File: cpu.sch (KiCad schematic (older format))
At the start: 30 parts, among them P27 BDM, U1 MC9S12XDP512, X1 16MHz

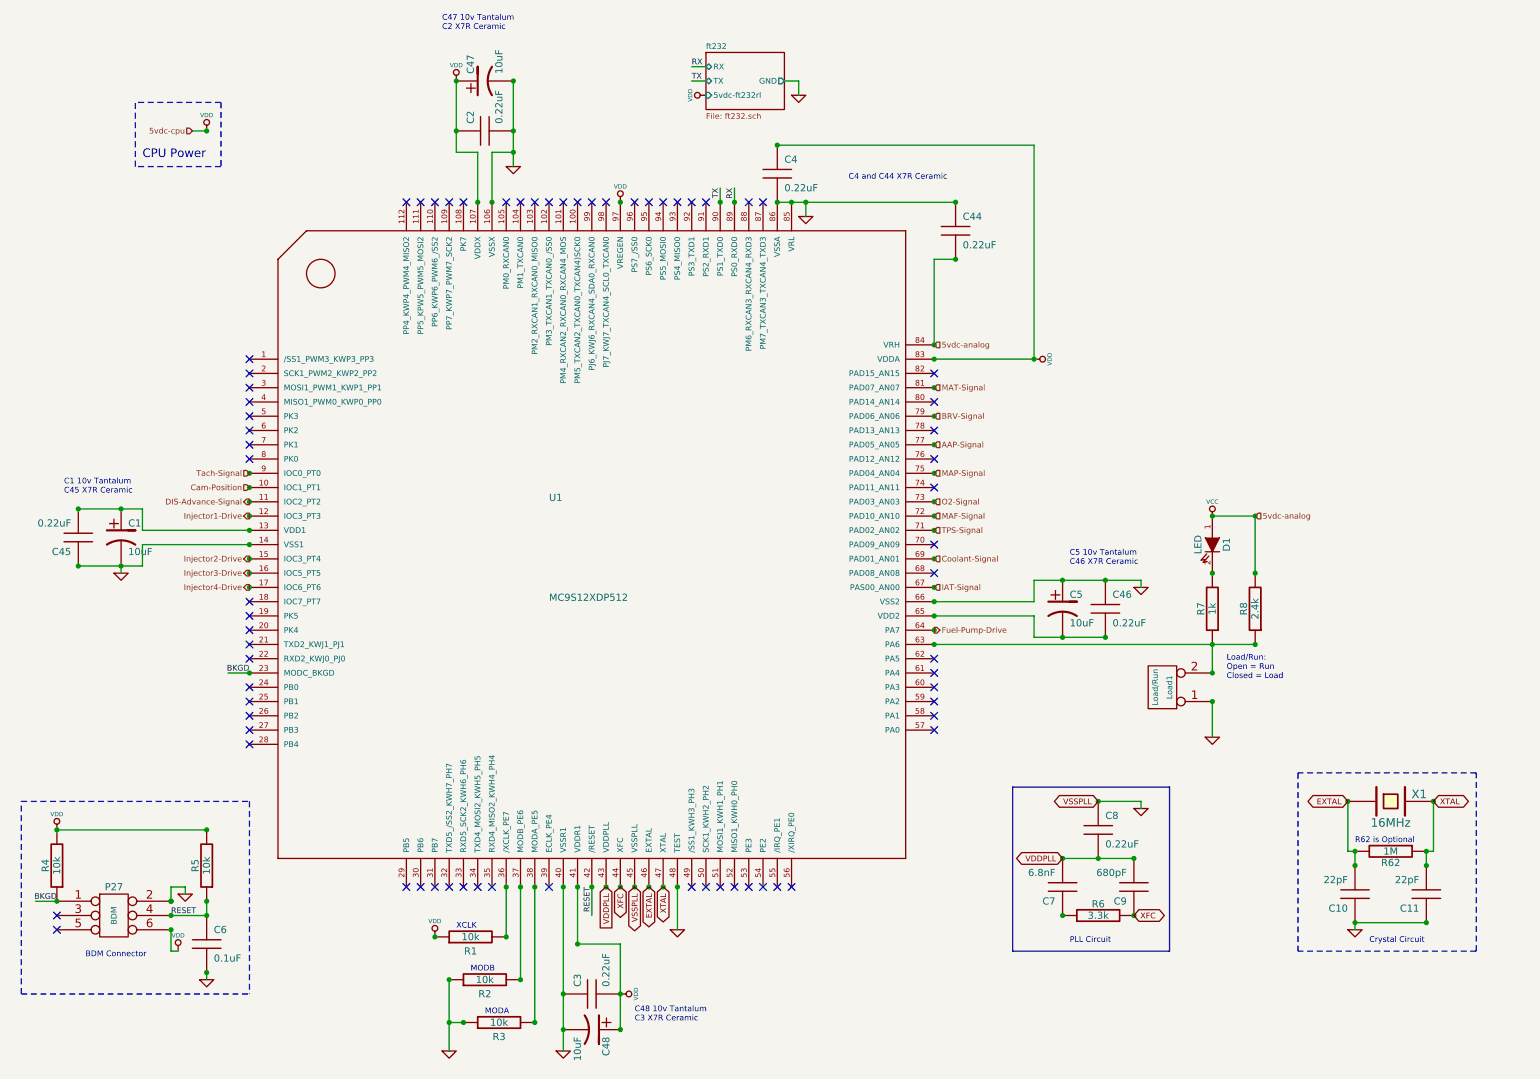
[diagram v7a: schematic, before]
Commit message: Schematics, PDF, BOM updated with latest changes
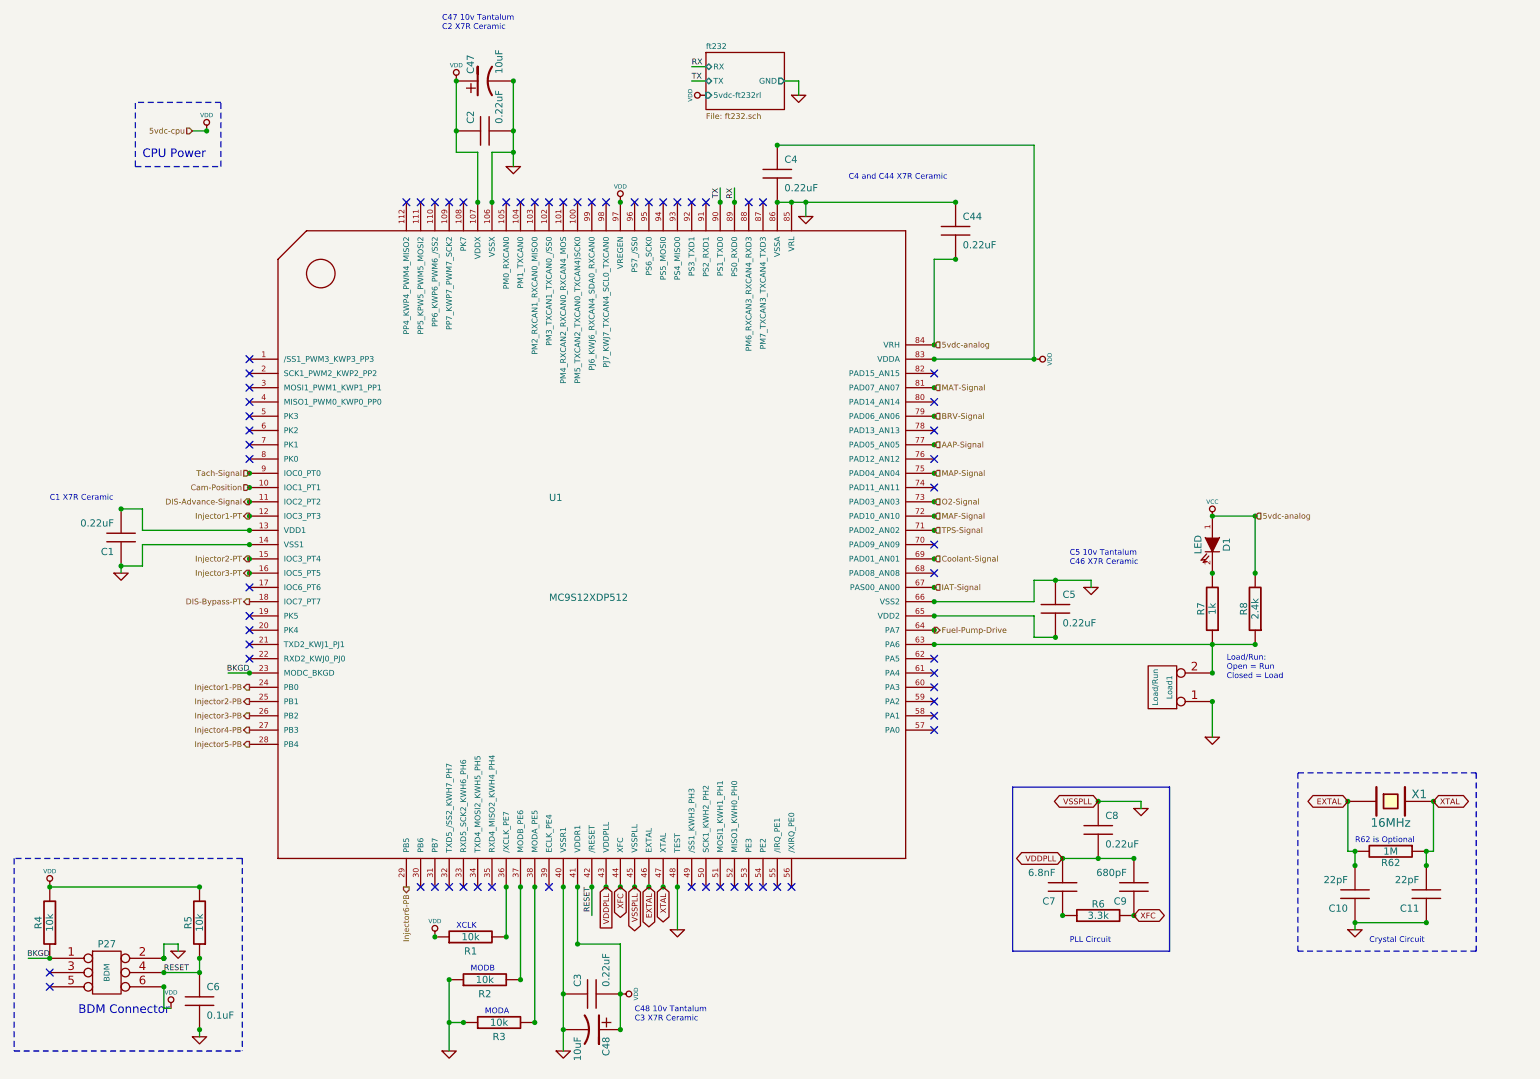
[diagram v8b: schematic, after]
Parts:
- removed C1, C5: 10uF, symbol CP1
- renumbered C45 to C1, C46 to C5
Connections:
- net labels added: DIS-Bypass-PT, Injector1-PB, Injector1-PT, Injector2-PB, Injector2-PT, Injector3-PB, Injector3-PT, Injector4-PB, Injector5-PB, Injector6-PB
- net labels removed: Injector1-Drive, Injector2-Drive, Injector3-Drive, Injector4-Drive
- no-connect marks 70 -> 64
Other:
- note added: "C1 X7R Ceramic"
- note removed: "C1 10v Tantalum\nC45 X7R Ceramic"
- moved on the sheet: C1, C5, C6, P27, R4, R5
